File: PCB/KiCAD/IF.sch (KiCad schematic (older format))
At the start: 34 parts, among them J2 JACK_TRS_3pins, P4 CONN_01X01, P5 CONN_01X01, P6 CONN_01X01, P7 CONN_01X01, Q6 MMBFJ310L, U1 NE5532, U4 LM78L06, U5 SA612

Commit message: mixer schema is done, pcb progress, fix 78l06 issue
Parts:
- removed U4: LM78L06, DragonFly:TO-92_Molded_Wide_Oval, symbol LM78L05
- added U4: L78L06_TO92, DragonFly:TO-92_Molded_Wide_Oval, symbol L78L06_TO92
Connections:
- net GND: now also U4.2 (GND)
- net RX_12V: now also U4.3 (VI)
- net at C31.2, C34.1, U5.8 (VCC): now also U4.1 (VO)
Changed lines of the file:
@@
 $EndComp
 $Comp
-L GND #PWR69
+L GND #PWR64
 U 1 1 58912103
 P 7700 2550
-F 0 "#PWR69" H 7700 2300 50  0001 C CNN
+F 0 "#PWR64" H 7700 2300 50  0001 C CNN
 F 1 "GND" H 7700 2400 50  0001 C CNN
 F 2 "" H 7700 2550 50  0000 C CNN
@@
 $EndComp
 $Comp
-L GND #PWR70
+L GND #PWR65
 U 1 1 58912546
 P 7700 2750
-F 0 "#PWR70" H 7700 2500 50  0001 C CNN
+F 0 "#PWR65" H 7700 2500 50  0001 C CNN
 F 1 "GND" H 7700 2600 50  0001 C CNN
 F 2 "" H 7700 2750 50  0000 C CNN
@@
 $EndComp
 $Comp
-L GND #PWR71
+L GND #PWR66
 U 1 1 58912989
 P 7700 2950
-F 0 "#PWR71" H 7700 2700 50  0001 C CNN
+F 0 "#PWR66" H 7700 2700 50  0001 C CNN
 F 1 "GND" H 7700 2800 50  0001 C CNN
 F 2 "" H 7700 2950 50  0000 C CNN
@@
 $EndComp
 $Comp
-L GND #PWR72
+L GND #PWR67
 U 1 1 589132CC
 P 7700 3150
-F 0 "#PWR72" H 7700 2900 50  0001 C CNN
+F 0 "#PWR67" H 7700 2900 50  0001 C CNN
 F 1 "GND" H 7700 3000 50  0001 C CNN
 F 2 "" H 7700 3150 50  0000 C CNN
@@
 $EndComp
 $Comp
-L GND #PWR59
+L GND #PWR54
 U 1 1 58AF70A6
 P 3000 3300
-F 0 "#PWR59" H 3000 3050 50  0001 C CNN
+F 0 "#PWR54" H 3000 3050 50  0001 C CNN
 F 1 "GND" H 3000 3150 50  0001 C CNN
 F 2 "" H 3000 3300 50  0000 C CNN
@@
 $EndComp
 $Comp
-L GND #PWR56
+L GND #PWR51
 U 1 1 58B15E5F
 P 2250 5000
-F 0 "#PWR56" H 2250 4750 50  0001 C CNN
+F 0 "#PWR51" H 2250 4750 50  0001 C CNN
 F 1 "GND" H 2250 4850 50  0001 C CNN
 F 2 "" H 2250 5000 50  0000 C CNN
@@
 $EndComp
 $Comp
-L LM78L05 U4
-U 1 1 58AF5A88
-P 3000 3050
-F 0 "U4" H 3000 3350 50  0000 C CNN
-F 1 "LM78L06" H 3000 3250 50  0000 C CNN
-F 2 "DragonFly:TO-92_Molded_Wide_Oval" H 3000 3050 50  0001 C CNN
-F 3 "" H 3000 3050 50  0000 C CNN
-	1    3000 3050
-	1    0    0    -1
-$EndComp
-$Comp
-L GND #PWR53
+L GND #PWR48
 U 1 1 58B0B2EB
 P 1400 5000
-F 0 "#PWR53" H 1400 4750 50  0001 C CNN
+F 0 "#PWR48" H 1400 4750 50  0001 C CNN
 F 1 "GND" H 1400 4850 50  0001 C CNN
 F 2 "" H 1400 5000 50  0000 C CNN
@@
 $EndComp
 $Comp
-L GND #PWR54
+L GND #PWR49
 U 1 1 58B0BE25
 P 1950 3250
-F 0 "#PWR54" H 1950 3000 50  0001 C CNN
+F 0 "#PWR49" H 1950 3000 50  0001 C CNN
 F 1 "GND" H 1950 3100 50  0001 C CNN
 F 2 "" H 1950 3250 50  0000 C CNN
@@
 $EndComp
 $Comp
-L GND #PWR55
+L GND #PWR50
 U 1 1 58B02D08
 P 2100 5000
-F 0 "#PWR55" H 2100 4750 50  0001 C CNN
+F 0 "#PWR50" H 2100 4750 50  0001 C CNN
 F 1 "GND" H 2100 4850 50  0001 C CNN
 F 2 "" H 2100 5000 50  0000 C CNN
@@
 $EndComp
 $Comp
-L GND #PWR58
+L GND #PWR53
 U 1 1 58B09A3F
 P 2700 4450
-F 0 "#PWR58" H 2700 4200 50  0001 C CNN
+F 0 "#PWR53" H 2700 4200 50  0001 C CNN
 F 1 "GND" H 2700 4300 50  0001 C CNN
 F 2 "" H 2700 4450 50  0000 C CNN
@@
 $EndComp
 $Comp
-L GND #PWR60
+L GND #PWR55
 U 1 1 58B399E4
 P 3650 3300
-F 0 "#PWR60" H 3650 3050 50  0001 C CNN
+F 0 "#PWR55" H 3650 3050 50  0001 C CNN
 F 1 "GND" H 3650 3150 50  0001 C CNN
 F 2 "" H 3650 3300 50  0000 C CNN
@@
 $EndComp
 $Comp
-L GND #PWR61
+L GND #PWR56
 U 1 1 58B39C92
 P 3850 3300
-F 0 "#PWR61" H 3850 3050 50  0001 C CNN
+F 0 "#PWR56" H 3850 3050 50  0001 C CNN
 F 1 "GND" H 3850 3150 50  0001 C CNN
 F 2 "" H 3850 3300 50  0000 C CNN
@@
 $EndComp
 $Comp
-L GND #PWR57
+L GND #PWR52
 U 1 1 58B3CA01
 P 2550 4200
-F 0 "#PWR57" H 2550 3950 50  0001 C CNN
+F 0 "#PWR52" H 2550 3950 50  0001 C CNN
 F 1 "GND" H 2550 4050 50  0001 C CNN
 F 2 "" H 2550 4200 50  0000 C CNN
@@
 $EndComp
 $Comp
-L GND #PWR63
+L GND #PWR58
 U 1 1 60FB6B9C
 P 4900 3500
-F 0 "#PWR63" H 4900 3250 50  0001 C CNN
+F 0 "#PWR58" H 4900 3250 50  0001 C CNN
 F 1 "GND" H 4900 3350 50  0001 C CNN
 F 2 "" H 4900 3500 50  0000 C CNN
@@
 $EndComp
 $Comp
-L GND #PWR62
+L GND #PWR57
 U 1 1 60FB7F45
 P 4550 4200
-F 0 "#PWR62" H 4550 3950 50  0001 C CNN
+F 0 "#PWR57" H 4550 3950 50  0001 C CNN
 F 1 "GND" H 4550 4050 50  0001 C CNN
 F 2 "" H 4550 4200 50  0000 C CNN
@@
 $EndComp
 $Comp
-L GND #PWR74
+L GND #PWR69
 U 1 1 60FB9C6F
 P 9550 5600
-F 0 "#PWR74" H 9550 5350 50  0001 C CNN
+F 0 "#PWR69" H 9550 5350 50  0001 C CNN
 F 1 "GND" H 9550 5450 50  0001 C CNN
 F 2 "" H 9550 5600 50  0000 C CNN
@@
 Connection ~ 6700 5000
 $Comp
-L GND #PWR73
+L GND #PWR68
 U 1 1 6123D132
 P 7850 5400
-F 0 "#PWR73" H 7850 5150 50  0001 C CNN
+F 0 "#PWR68" H 7850 5150 50  0001 C CNN
 F 1 "GND" H 7850 5250 50  0001 C CNN
 F 2 "" H 7850 5400 50  0000 C CNN
@@
 	3000 4900 5400 4900
 Wire Wire Line
-	1950 3000 2600 3000
+	1950 3000 2700 3000
 Connection ~ 2250 3000
 Wire Wire Line
@@
 $EndComp
 $Comp
-L GND #PWR64
+L GND #PWR59
 U 1 1 61240985
 P 4950 5250
-F 0 "#PWR64" H 4950 5000 50  0001 C CNN
+F 0 "#PWR59" H 4950 5000 50  0001 C CNN
 F 1 "GND" H 4950 5100 50  0001 C CNN
 F 2 "" H 4950 5250 50  0000 C CNN
@@
 $EndComp
 $Comp
-L GND #PWR67
+L GND #PWR62
 U 1 1 61240A0C
 P 5600 5300
-F 0 "#PWR67" H 5600 5050 50  0001 C CNN
+F 0 "#PWR62" H 5600 5050 50  0001 C CNN
 F 1 "GND" H 5600 5150 50  0001 C CNN
 F 2 "" H 5600 5300 50  0000 C CNN
@@
 Connection ~ 7200 4900
 $Comp
-L GND #PWR68
+L GND #PWR63
 U 1 1 61241D9A
 P 7200 5200
-F 0 "#PWR68" H 7200 4950 50  0001 C CNN
+F 0 "#PWR63" H 7200 4950 50  0001 C CNN
 F 1 "GND" H 7200 5050 50  0001 C CNN
 F 2 "" H 7200 5200 50  0000 C CNN
@@
 	5250 5850 5250 5950
 $Comp
-L GND #PWR66
+L GND #PWR61
 U 1 1 61243457
 P 5250 6350
-F 0 "#PWR66" H 5250 6100 50  0001 C CNN
+F 0 "#PWR61" H 5250 6100 50  0001 C CNN
 F 1 "GND" H 5250 6200 50  0001 C CNN
 F 2 "" H 5250 6350 50  0000 C CNN
@@
 	7850 4550 7850 4700
 $Comp
-L GND #PWR65
+L GND #PWR60
 U 1 1 61244C87
 P 5100 4550
-F 0 "#PWR65" H 5100 4300 50  0001 C CNN
+F 0 "#PWR60" H 5100 4300 50  0001 C CNN
 F 1 "GND" H 5100 4400 50  0001 C CNN
 F 2 "" H 5100 4550 50  0000 C CNN
@@
 	5100 4550 5200 4550
 Wire Wire Line
-	3400 3000 4300 3000
+	3300 3000 4300 3000
 Wire Wire Line
 	3650 3000 3650 3100
@@
 	1    0    0    1
 $EndComp
+$Comp
+L L78L06_TO92 U4
+U 1 1 612CC039
+P 3000 3000
+F 0 "U4" H 2800 3300 50  0000 C CNN
+F 1 "L78L06_TO92" H 2750 3200 50  0000 L CNN
+F 2 "DragonFly:TO-92_Molded_Wide_Oval" H 3000 3225 50  0001 C CIN
+F 3 "" H 3000 2950 50  0001 C CNN
+	1    3000 3000
+	1    0    0    -1
+$EndComp
 $EndSCHEMATC

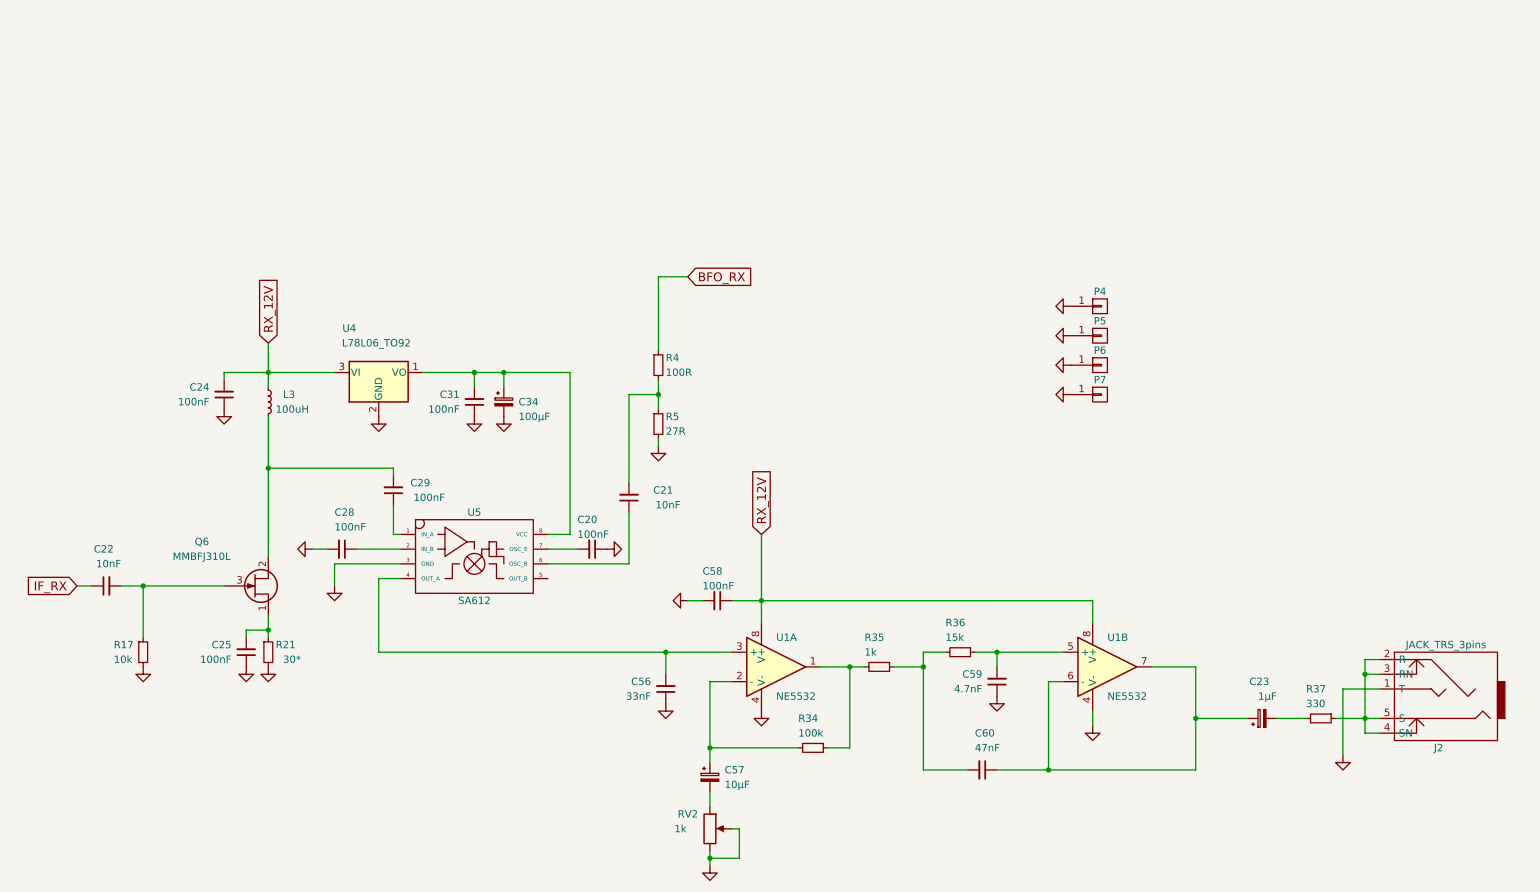
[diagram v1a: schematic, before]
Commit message: add AGC circuit
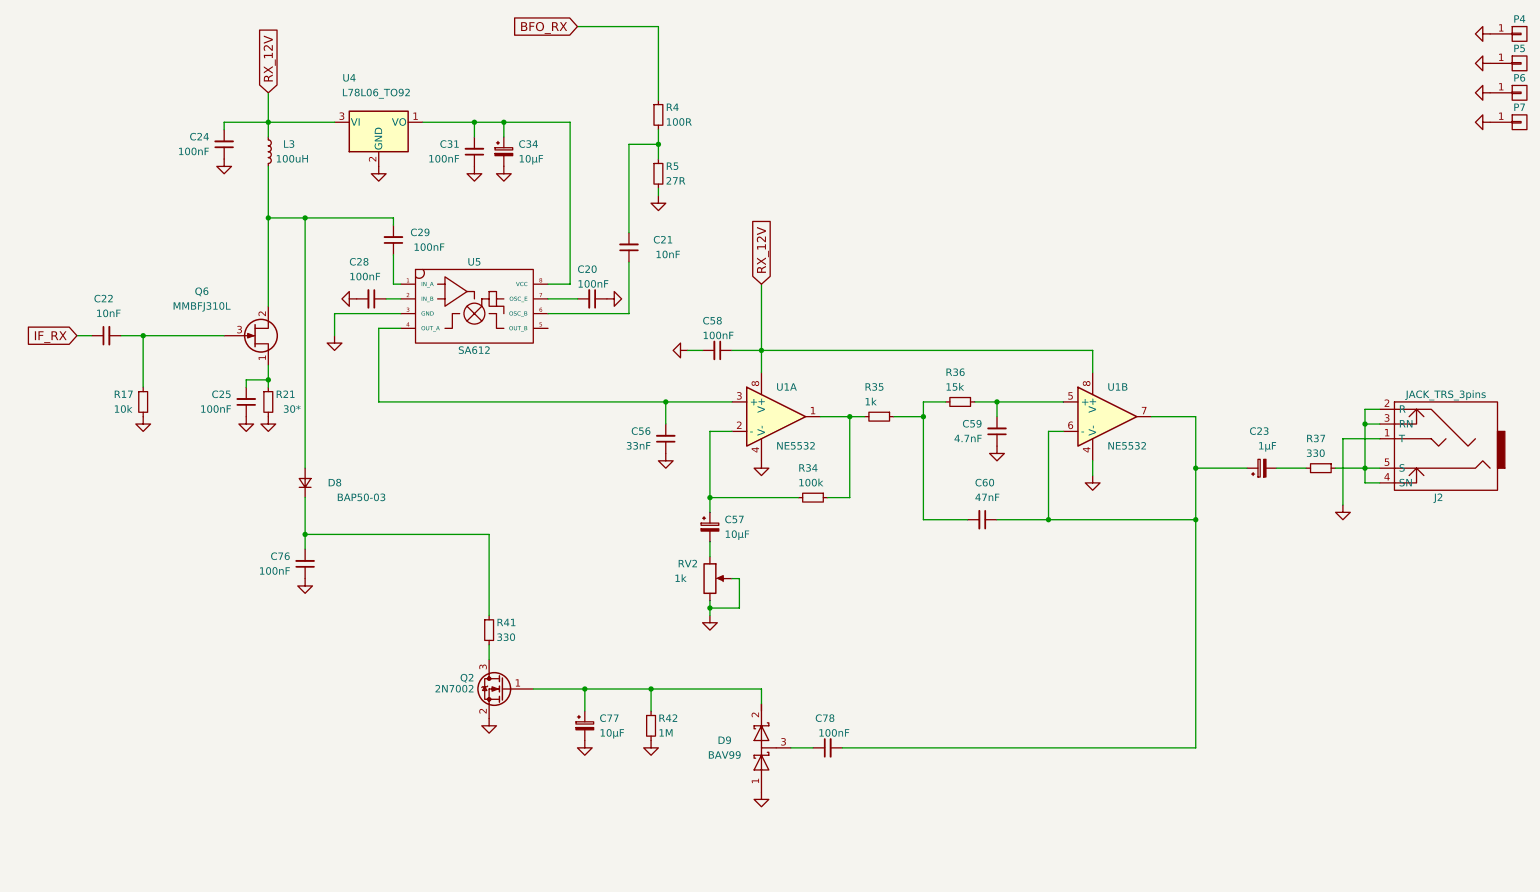
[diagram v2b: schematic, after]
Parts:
- added C76: 100nF, DragonFly:C_0603_HandSoldering, symbol C_Small
- added C77: 10µF, DragonFly:CP_Radial_D4.0mm_P2.00mm, symbol CP_Small
- added C78: 100nF, Capacitors_SMD:C_0603_HandSoldering, symbol C_Small
- added D8: BAP50-03, DragonFly:D_SOD-323_HandSoldering, symbol D_Small
- added D9: BAV99, DragonFly:SOT-23, symbol D_Schottky_x2_Serial_AKC
- added Q2: 2N7002, DragonFly:SOT-23, symbol 2N7002
- added R41: 330, DragonFly:R_1206_0603, symbol R_Small
- added R42: 1M, DragonFly:R_1206_0603, symbol R_Small
- C34: value 100µF -> 10µF; footprint DragonFly:CP_Radial_D6.3mm_P2.50mm -> DragonFly:CP_Radial_D4.0mm_P2.00mm
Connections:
- net GND: now also C76.1, C77.2, D9.1 (A), Q2.2 (S), R42.2
- net at C29.2, L3.2, Q6.2 (S): now also D8.2 (A)
- net at C23.1, C60.1, U1.6 (-)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: now also C78.2
- new net: C77.1, D9.2 (K), Q2.1 (G), R42.1
- new net: C78.1, D9.3 (common)
- new net: Q2.3 (D), R41.2
- new net: C76.2, D8.1 (K), R41.1
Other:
- moved on the sheet: C20, C21, C22, C23, C24, C25, C28, C29, C31, C56, C57, C58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
